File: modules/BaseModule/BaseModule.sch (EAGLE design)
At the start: 47 parts, among them IC1 AMS1117-5.0, J1 4P-2.0-90D, J2 4p-2.54

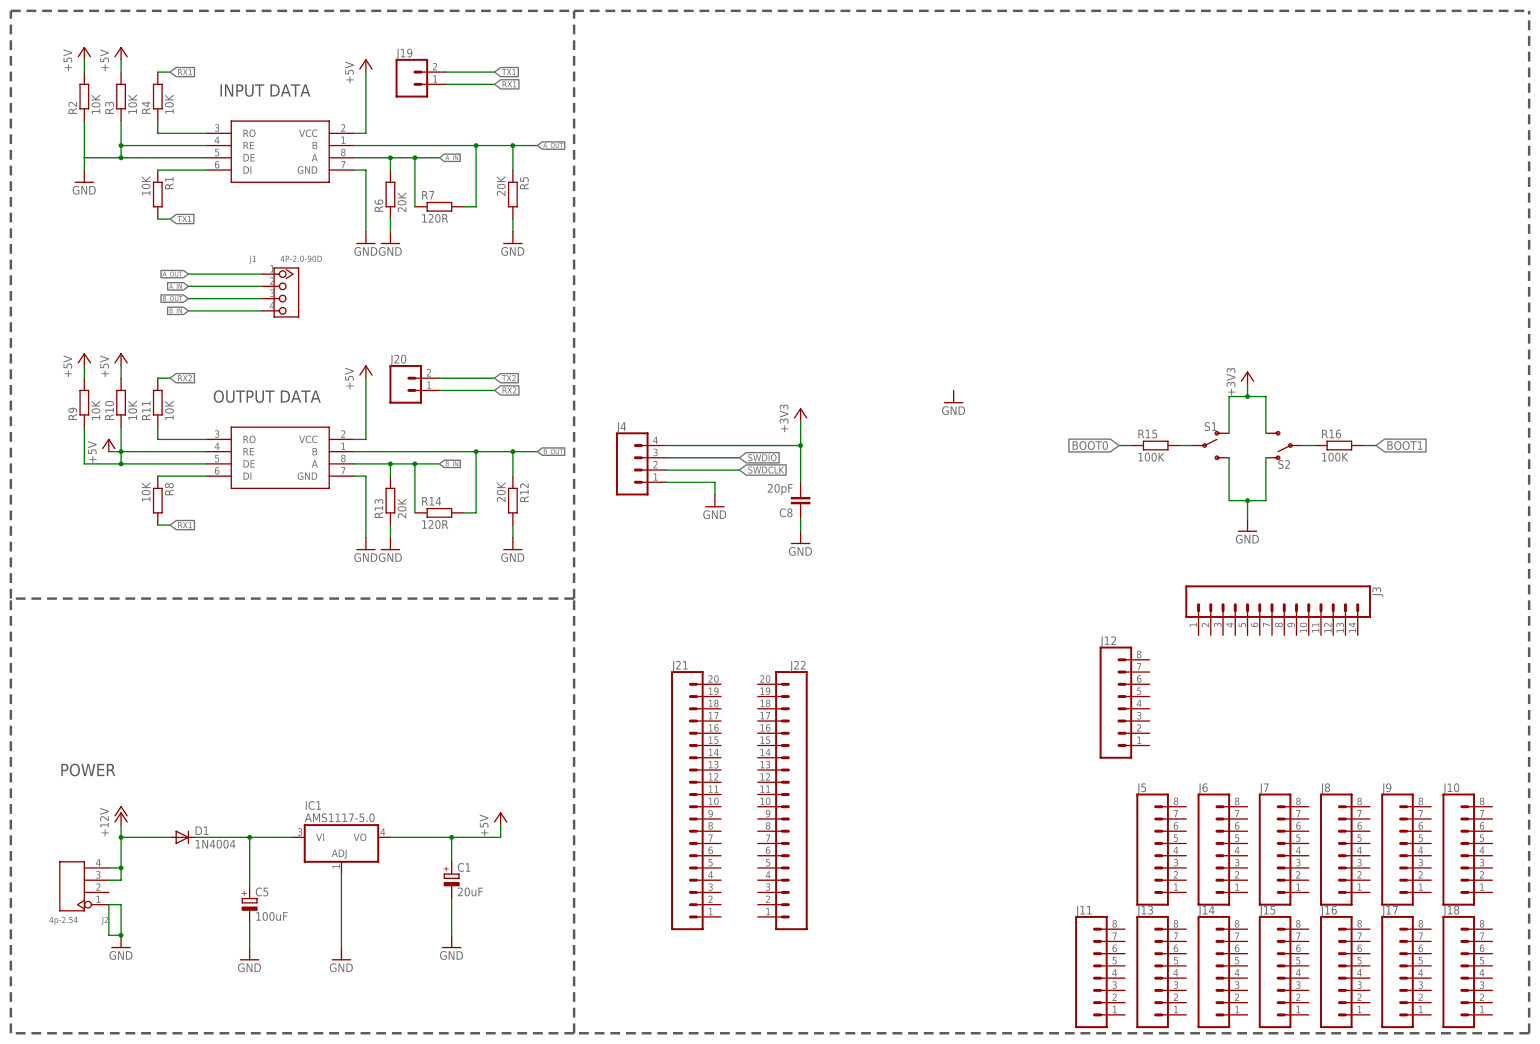
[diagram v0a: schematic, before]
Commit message: BaseModule pcb updates
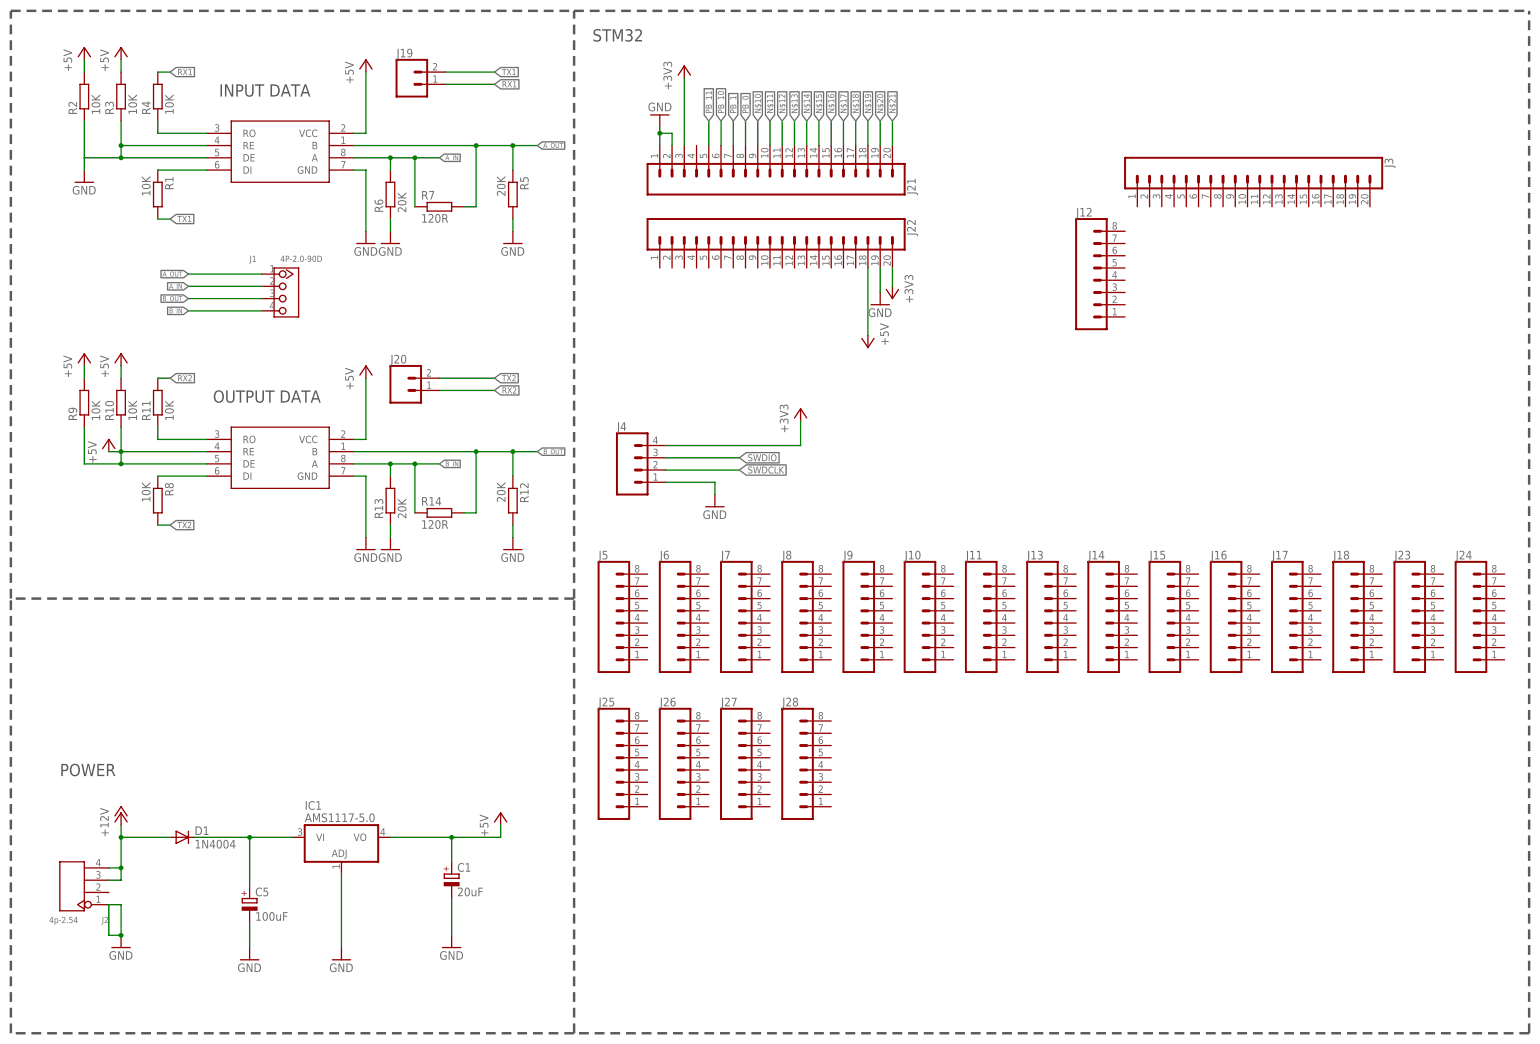
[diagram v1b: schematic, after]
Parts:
- removed C8: 20pF, rcl:C-EUC0805
- removed R15, R16: 100K, rcl:R-EU_R0805
- removed S1, S2: (no value), SparkFun-Switches:SWITCH-SPDT-PTH-11.6X4.0MM-LOCK
- added J23, J24, J25, J26, J27, J28: (no value), SparkFun-Connectors:CONN_08"
- J3: device SparkFun-Connectors:CONN_14 -> SparkFun-Connectors:CONN_20
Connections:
- removed net BOOT0: R15.1
- removed net BOOT1: R16.2
- removed net N$5: R15.2, S1.P
- removed net N$6: R16.1, S2.P
- new net N$10: J21.9
- new net N$11: J21.10
- new net N$12: J21.11
- new net N$13: J21.12
- new net N$14: J21.13
- new net N$15: J21.14
- new net N$16: J21.15
- new net N$17: J21.16
- new net N$18: J21.17
- new net N$19: J21.18
- new net N$20: J21.19
- new net N$21: J21.20
- new net PB_0: J21.8
- new net PB_1: J21.7
- new net PB_10: J21.6
- new net PB_11: J21.5
- net +3V3: now also J21.3, J22.20; no longer C8.2, S1.O, S2.S
- net +5V: now also J22.18
- net GND: now also J21.1, J21.2, J22.19; no longer C8.1, S1.S, S2.O
- net RX1: no longer R8.2
- net TX2: now also R8.2
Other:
- note added: "STM32"
- moved on the sheet: J10, J11, J12, J13, J14, J15, J16, J17, J18, J21, J22, J5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
